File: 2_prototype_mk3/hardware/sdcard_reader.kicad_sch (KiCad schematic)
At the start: 4 parts, among them J1 Micro_SD_Card

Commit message: MKIII design refinements
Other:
- title: (none) -> SD card reader
- moved on the sheet: C7, C8, J1, RN2

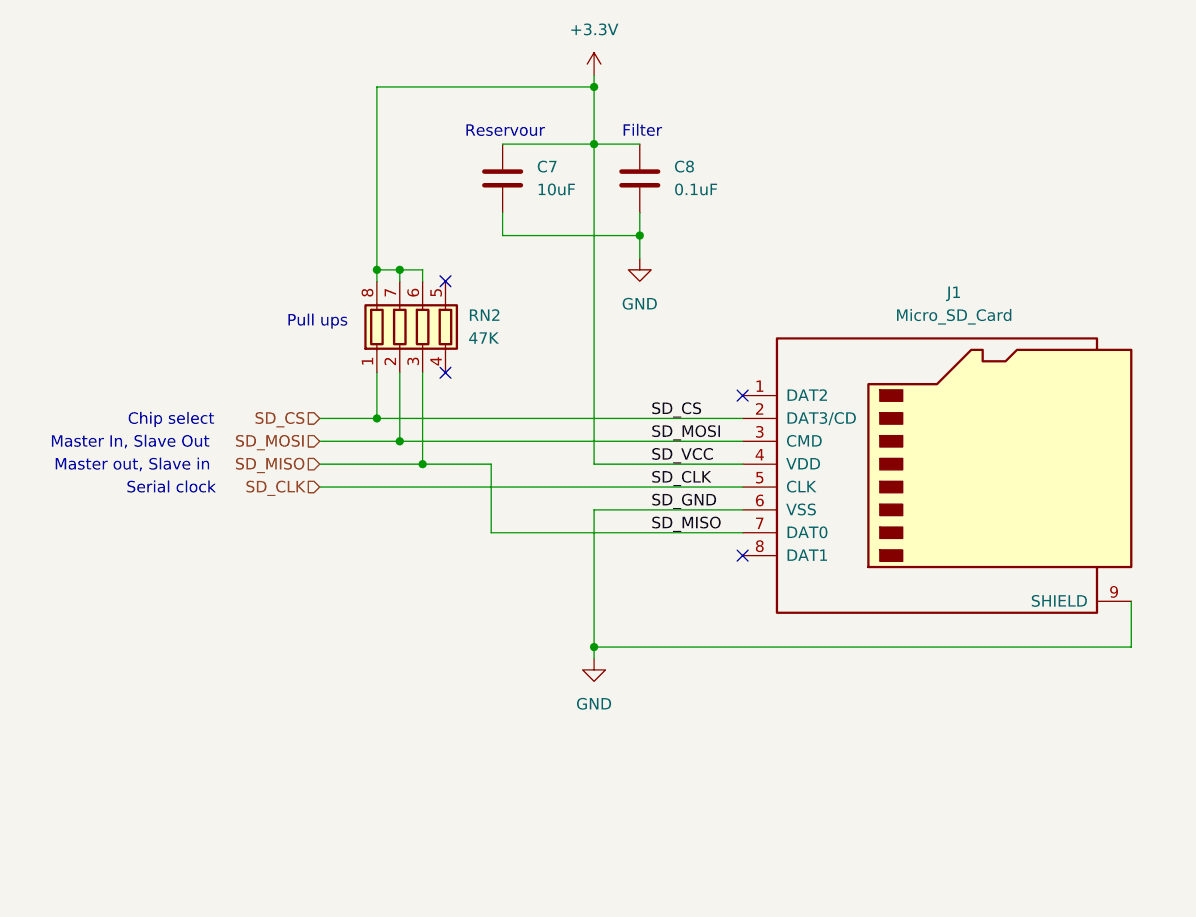
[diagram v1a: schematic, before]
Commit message: Add net classes for power
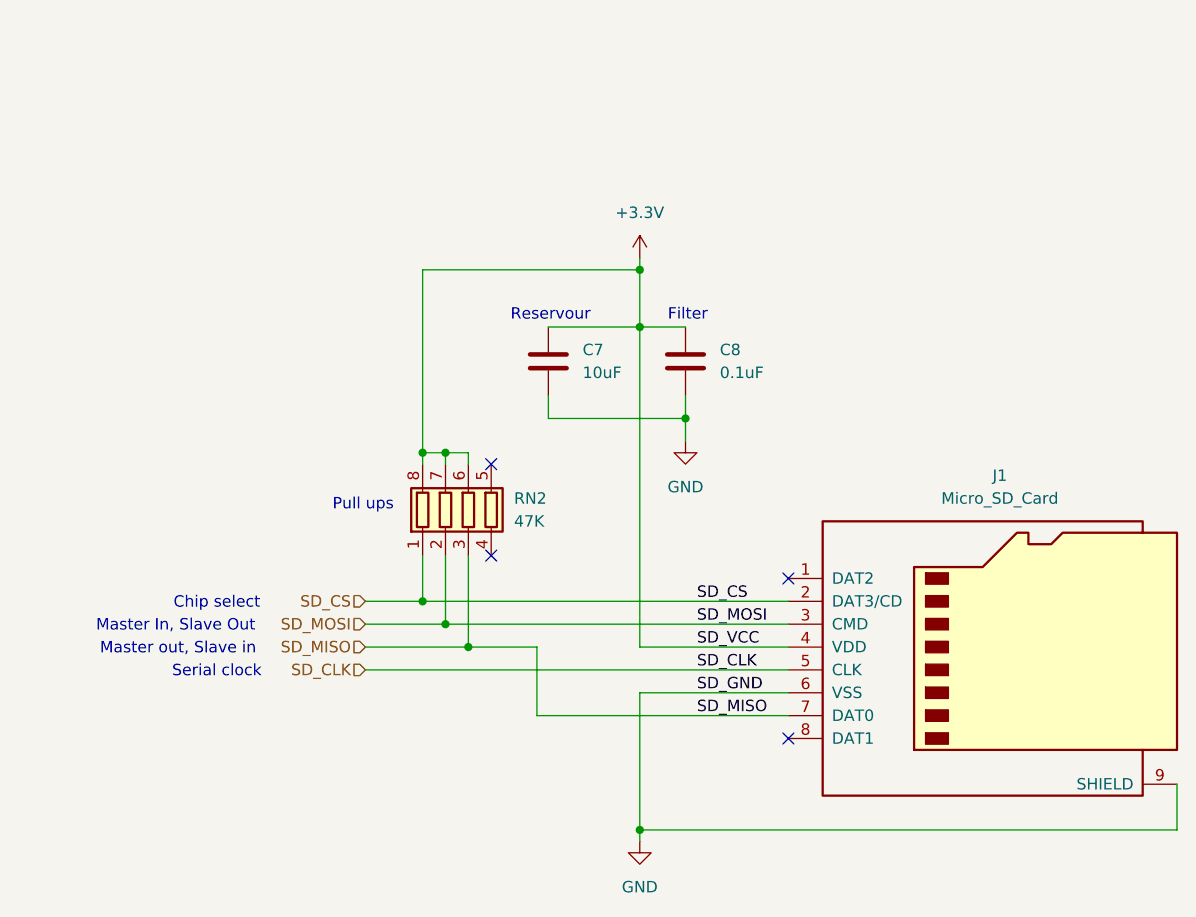
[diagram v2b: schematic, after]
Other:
- title: SD card reader -> (none)
- moved on the sheet: C7, C8, J1, RN2

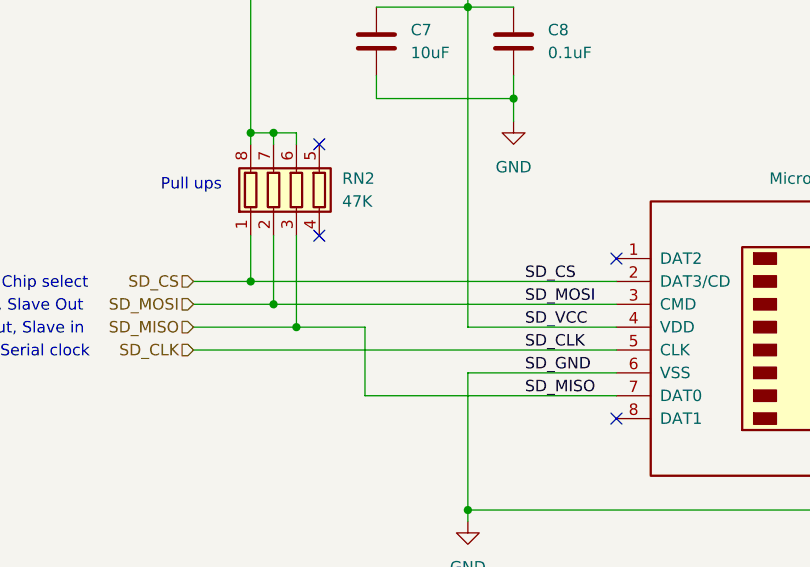
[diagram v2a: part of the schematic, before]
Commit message: MKIII PCB components connected and passing DRC
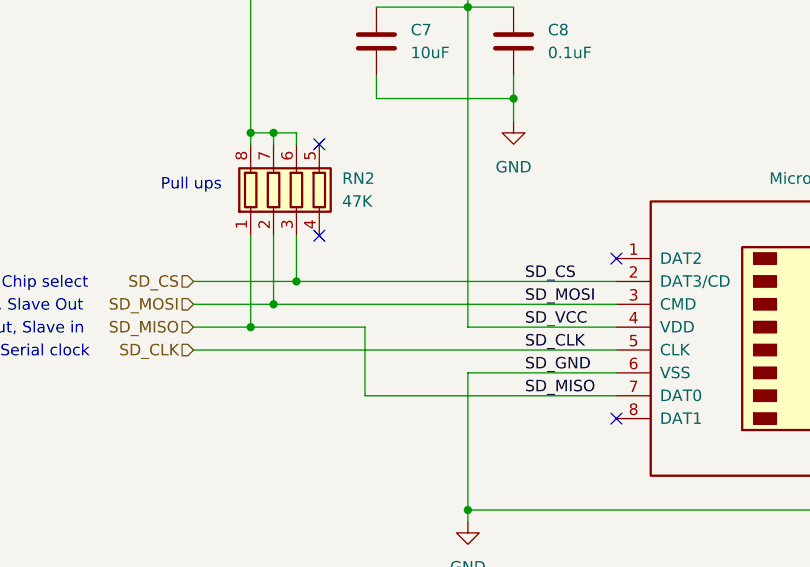
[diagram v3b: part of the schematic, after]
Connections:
- net SD_CS: now also RN2.3 (R3.1); no longer RN2.1 (R1.1)
- net SD_MISO: now also RN2.1 (R1.1); no longer RN2.3 (R3.1)
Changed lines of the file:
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@@
 	)
 	(junction
-		(at 83.82 87.63)
+		(at 88.9 87.63)
+		(diameter 0)
+		(color 0 0 0 0)
+	)
+	(junction
+		(at 83.82 92.71)
 		(diameter 0)
 		(color 0 0 0 0)
@@
 	(junction
 		(at 83.82 71.12)
-		(diameter 0)
-		(color 0 0 0 0)
-	)
-	(junction
-		(at 88.9 92.71)
 		(diameter 0)
 		(color 0 0 0 0)
@@
 	(wire
 		(pts
-			(xy 83.82 82.55) (xy 83.82 87.63)
-		)
-		(stroke
-			(width 0)
-			(type default)
-		)
-	)
-	(wire
-		(pts
 			(xy 96.52 92.71) (xy 96.52 100.33)
 		)
@@
 	(wire
 		(pts
+			(xy 83.82 82.55) (xy 83.82 92.71)
+		)
+		(stroke
+			(width 0)
+			(type default)
+		)
+	)
+	(wire
+		(pts
 			(xy 113.03 64.77) (xy 113.03 67.31)
 		)
@@
 	(wire
 		(pts
+			(xy 88.9 82.55) (xy 88.9 87.63)
+		)
+		(stroke
+			(width 0)
+			(type default)
+		)
+	)
+	(wire
+		(pts
 			(xy 107.95 113.03) (xy 167.64 113.03)
 		)
@@
 	(wire
 		(pts
-			(xy 77.47 92.71) (xy 88.9 92.71)
+			(xy 77.47 92.71) (xy 83.82 92.71)
 		)
 		(stroke
@@
 	(wire
 		(pts
-			(xy 83.82 87.63) (xy 124.46 87.63)
-		)
-		(stroke
-			(width 0)
-			(type default)
-		)
-	)
-	(wire
-		(pts
-			(xy 88.9 92.71) (xy 96.52 92.71)
+			(xy 83.82 92.71) (xy 96.52 92.71)
 		)
 		(stroke
@@
 	(wire
 		(pts
-			(xy 88.9 82.55) (xy 88.9 92.71)
-		)
-		(stroke
-			(width 0)
-			(type default)
-		)
-	)
-	(wire
-		(pts
 			(xy 113.03 67.31) (xy 113.03 69.85)
 		)
@@
 	(wire
 		(pts
-			(xy 77.47 87.63) (xy 83.82 87.63)
-		)
-		(stroke
+			(xy 77.47 87.63) (xy 88.9 87.63)
+		)
+		(stroke
+			(width 0)
+			(type default)
+		)
+	)
+	(wire
+		(pts
+			(xy 88.9 87.63) (xy 124.46 87.63)
+		)
+		(stroke

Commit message: Add manufacturer part nu bers
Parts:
- C7: Manufacturer_Part_Number (none) -> CL31A106KAHNNNE
- C8: Manufacturer_Part_Number (none) -> CL10B104KO8NNNC
- J1: Manufacturer_Part_Number (none) -> 104031-0811
- RN2: Manufacturer_Part_Number (none) -> YC164-JR-0747KL
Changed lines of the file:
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@@
+			)
+		)
+		(property "Manufacturer_Part_Number" "YC164-JR-0747KL"
+			(at 88.9 77.47 0)
+			(effects
+				(font
+					(size 1.27 1.27)
+				)
+				(hide yes)
 			)
 		)
@@
 			)
 		)
+		(property "Manufacturer_Part_Number" "CL10B104KO8NNNC"
+			(at 113.03 60.96 0)
+			(effects
+				(font
+					(size 1.27 1.27)
+				)
+				(hide yes)
+			)
+		)
 		(pin "2"
 		)
@@
 			)
 		)
+		(property "Manufacturer_Part_Number" "104031-0811"
+			(at 147.32 92.71 0)
+			(effects
+				(font
+					(size 1.27 1.27)
+				)
+				(hide yes)
+			)
+		)
 		(pin "2"
 		)
@@
 			(at 97.79 60.96 0)
 			(effects
+				(font
+					(size 1.27 1.27)
+				)
+				(hide yes)
+			)
+		)
+		(property "Manufacturer_Part_Number" "CL31A106KAHNNNE"
+			(at 97.79 60.96 0)
+			(effects

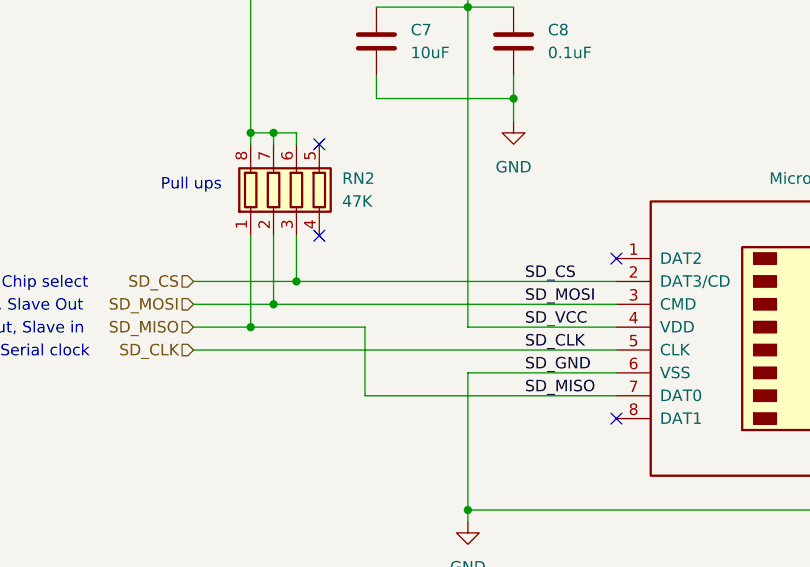
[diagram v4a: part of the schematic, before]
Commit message: Switch SD card reader to better component
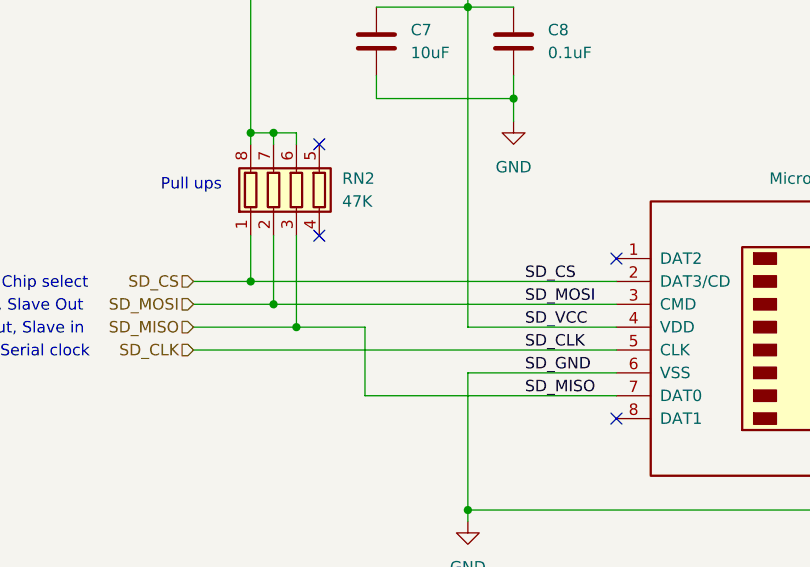
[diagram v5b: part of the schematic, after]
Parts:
- J1: footprint Connector_Card:microSD_HC_Molex_104031-0811 -> Connector_Card:microSD_HC_Hirose_DM3D-SF; Manufacturer_Part_Number 104031-0811 -> DM3D-SF
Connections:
- net SD_CS: now also RN2.1 (R1.1); no longer RN2.3 (R3.1)
- net SD_MISO: now also RN2.3 (R3.1); no longer RN2.1 (R1.1)
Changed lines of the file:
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@@
 	)
 	(junction
-		(at 88.9 87.63)
-		(diameter 0)
-		(color 0 0 0 0)
-	)
-	(junction
-		(at 83.82 92.71)
+		(at 83.82 87.63)
 		(diameter 0)
 		(color 0 0 0 0)
@@
 		(color 0 0 0 0)
 	)
+	(junction
+		(at 88.9 92.71)
+		(diameter 0)
+		(color 0 0 0 0)
+	)
 	(no_connect
 		(at 91.44 82.55)
@@
 	(wire
 		(pts
+			(xy 88.9 82.55) (xy 88.9 92.71)
+		)
+		(stroke
+			(width 0)
+			(type default)
+		)
+	)
+	(wire
+		(pts
 			(xy 97.79 57.15) (xy 107.95 57.15)
 		)
@@
 	(wire
 		(pts
-			(xy 83.82 82.55) (xy 83.82 92.71)
-		)
-		(stroke
-			(width 0)
-			(type default)
-		)
-	)
-	(wire
-		(pts
 			(xy 113.03 64.77) (xy 113.03 67.31)
 		)
@@
 	(wire
 		(pts
-			(xy 88.9 82.55) (xy 88.9 87.63)
-		)
-		(stroke
-			(width 0)
-			(type default)
-		)
-	)
-	(wire
-		(pts
 			(xy 107.95 113.03) (xy 167.64 113.03)
 		)
@@
 	(wire
 		(pts
+			(xy 88.9 92.71) (xy 96.52 92.71)
+		)
+		(stroke
+			(width 0)
+			(type default)
+		)
+	)
+	(wire
+		(pts
 			(xy 107.95 97.79) (xy 107.95 113.03)
 		)
@@
 	(wire
 		(pts
+			(xy 83.82 87.63) (xy 124.46 87.63)
+		)
+		(stroke
+			(width 0)
+			(type default)
+		)
+	)
+	(wire
+		(pts
 			(xy 124.46 97.79) (xy 107.95 97.79)
 		)
@@
 	(wire
 		(pts
-			(xy 77.47 92.71) (xy 83.82 92.71)
+			(xy 77.47 92.71) (xy 88.9 92.71)
 		)
 		(stroke
@@
 	(wire
 		(pts
-			(xy 83.82 92.71) (xy 96.52 92.71)
+			(xy 83.82 82.55) (xy 83.82 87.63)
 		)
 		(stroke
@@
 	(wire
 		(pts
-			(xy 77.47 87.63) (xy 88.9 87.63)
-		)
-		(stroke
-			(width 0)
-			(type default)
-		)
-	)
-	(wire
-		(pts
-			(xy 88.9 87.63) (xy 124.46 87.63)
+			(xy 77.47 87.63) (xy 83.82 87.63)
 		)
 		(stroke
@@
 			)
 		)
-		(property "Footprint" "Connector_Card:microSD_HC_Molex_104031-0811"
+		(property "Footprint" "Connector_Card:microSD_HC_Hirose_DM3D-SF"
 			(at 176.53 85.09 0)
 			(effects
@@
 			)
 		)
-		(property "Datasheet" "https://www.we-online.com/components/products/datasheet/693072010801.pdf"
+		(property "Datasheet" ""
 			(at 147.32 92.71 0)
 			(effects
@@
 			)
 		)
-		(property "Manufacturer_Part_Number" "104031-0811"
+		(property "Manufacturer_Part_Number" "DM3D-SF"
 			(at 147.32 92.71 0)
 			(effects

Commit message: Fix DRC issues and change SD card to injection model
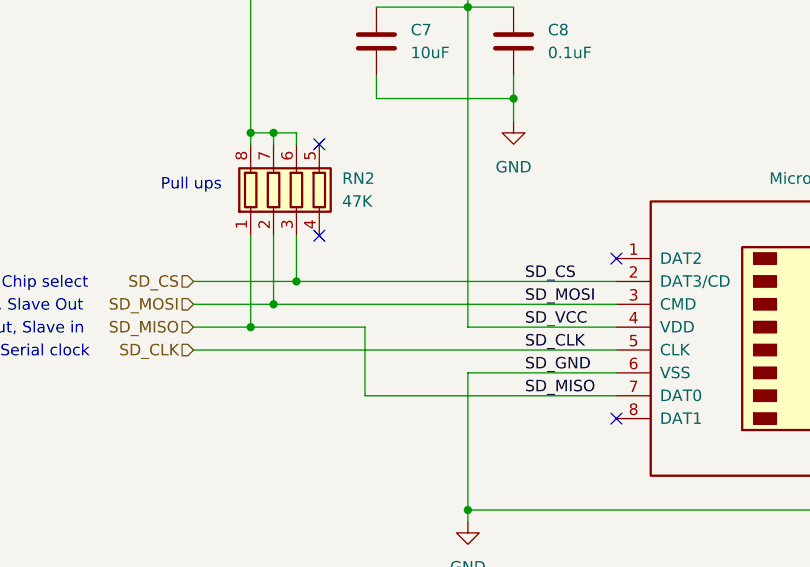
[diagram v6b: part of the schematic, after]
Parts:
- J1: footprint Connector_Card:microSD_HC_Hirose_DM3D-SF -> Connector_Card:microSD_HC_Hirose_DM3AT-SF-PEJM5
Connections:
- net SD_CS: now also RN2.3 (R3.1); no longer RN2.1 (R1.1)
- net SD_MISO: now also RN2.1 (R1.1); no longer RN2.3 (R3.1)
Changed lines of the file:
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@@
 	)
 	(junction
-		(at 83.82 87.63)
+		(at 88.9 87.63)
 		(diameter 0)
 		(color 0 0 0 0)
@@
 	)
 	(junction
+		(at 83.82 92.71)
+		(diameter 0)
+		(color 0 0 0 0)
+	)
+	(junction
 		(at 86.36 71.12)
 		(diameter 0)
@@
 		(color 0 0 0 0)
 	)
-	(junction
-		(at 88.9 92.71)
-		(diameter 0)
-		(color 0 0 0 0)
-	)
 	(no_connect
 		(at 91.44 82.55)
@@
 	(wire
 		(pts
-			(xy 88.9 82.55) (xy 88.9 92.71)
-		)
-		(stroke
-			(width 0)
-			(type default)
-		)
-	)
-	(wire
-		(pts
 			(xy 97.79 57.15) (xy 107.95 57.15)
 		)
@@
 	(wire
 		(pts
-			(xy 88.9 92.71) (xy 96.52 92.71)
-		)
-		(stroke
-			(width 0)
-			(type default)
-		)
-	)
-	(wire
-		(pts
 			(xy 107.95 97.79) (xy 107.95 113.03)
 		)
@@
 	(wire
 		(pts
-			(xy 83.82 87.63) (xy 124.46 87.63)
+			(xy 83.82 82.55) (xy 83.82 92.71)
 		)
 		(stroke
@@
 	(wire
 		(pts
-			(xy 77.47 92.71) (xy 88.9 92.71)
+			(xy 77.47 92.71) (xy 83.82 92.71)
 		)
 		(stroke
@@
 	(wire
 		(pts
-			(xy 83.82 82.55) (xy 83.82 87.63)
+			(xy 88.9 82.55) (xy 88.9 87.63)
 		)
 		(stroke
@@
 	(wire
 		(pts
-			(xy 77.47 87.63) (xy 83.82 87.63)
+			(xy 77.47 87.63) (xy 88.9 87.63)
+		)
+		(stroke
+			(width 0)
+			(type default)
+		)
+	)
+	(wire
+		(pts
+			(xy 83.82 92.71) (xy 96.52 92.71)
 		)
 		(stroke
@@
 		(pts
 			(xy 124.46 92.71) (xy 107.95 92.71)
+		)
+		(stroke
+			(width 0)
+			(type default)
+		)
+	)
+	(wire
+		(pts
+			(xy 88.9 87.63) (xy 124.46 87.63)
 		)
 		(stroke
@@
 			)
 		)
-		(property "Footprint" "Connector_Card:microSD_HC_Hirose_DM3D-SF"
+		(property "Footprint" "Connector_Card:microSD_HC_Hirose_DM3AT-SF-PEJM5"
 			(at 176.53 85.09 0)
 			(effects

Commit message: Add LCSC component part numbers to BOM
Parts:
- J1: Manufacturer (none) -> Hirose Electric
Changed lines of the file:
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@@
+			)
+		)
+		(property "Manufacturer" ""
+			(at 88.9 77.47 0)
+			(effects
+				(font
+					(size 1.27 1.27)
+				)
+				(hide yes)
 			)
 		)
@@
 			)
 		)
+		(property "Manufacturer" ""
+			(at 113.03 60.96 0)
+			(effects
+				(font
+					(size 1.27 1.27)
+				)
+				(hide yes)
+			)
+		)
 		(pin "2"
 		)
@@
 			)
 		)
+		(property "Manufacturer" "Hirose Electric"
+			(at 147.32 92.71 0)
+			(effects
+				(font
+					(size 1.27 1.27)
+				)
+				(hide yes)
+			)
+		)
 		(pin "2"
 		)
@@
 			(at 97.79 60.96 0)
 			(effects
+				(font
+					(size 1.27 1.27)
+				)
+				(hide yes)
+			)
+		)
+		(property "Manufacturer" ""
+			(at 97.79 60.96 0)
+			(effects

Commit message: Add LCSC components part numbers
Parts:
- J1: LCSC_Part_Number (none) -> C719027
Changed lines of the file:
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@@
+			)
+		)
+		(property "LCSC_Part_Number" ""
+			(at 88.9 77.47 0)
+			(effects
+				(font
+					(size 1.27 1.27)
+				)
+				(hide yes)
 			)
 		)
@@
 			)
 		)
+		(property "LCSC_Part_Number" ""
+			(at 113.03 60.96 0)
+			(effects
+				(font
+					(size 1.27 1.27)
+				)
+				(hide yes)
+			)
+		)
 		(pin "2"
 		)
@@
 			)
 		)
+		(property "LCSC_Part_Number" "C719027"
+			(at 147.32 92.71 0)
+			(effects
+				(font
+					(size 1.27 1.27)
+				)
+				(hide yes)
+			)
+		)
 		(pin "2"
 		)
@@
 			(at 97.79 60.96 0)
 			(effects
+				(font
+					(size 1.27 1.27)
+				)
+				(hide yes)
+			)
+		)
+		(property "LCSC_Part_Number" ""
+			(at 97.79 60.96 0)
+			(effects
